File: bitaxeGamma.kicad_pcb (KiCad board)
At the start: 4 copper layers, 56.5 x 99.8 mm, 131 parts, among them J1 54-00164, J2 TC2030-IDC, J3 Conn_01x04, J4 Conn_01x06, J5 USB_C_Receptacle_USB2.0, J6 Conn_01x04, J7 Conn_01x04, SW1 GT-TC029B-H025-L1N, SW2 GT-TC029B-H025-L1N, T1 net-tie, U10 EMC2101, U2 TPS546D24ARVFR, U3 RT9080-33GJ5, U4 ESP32-S3-WROOM-1, U5 MCP1824T-1202E/OT, U6 MCP1824T-0802E, U7 25MHz, U8 BM1370_mode1, U9 SN74AVC4T774

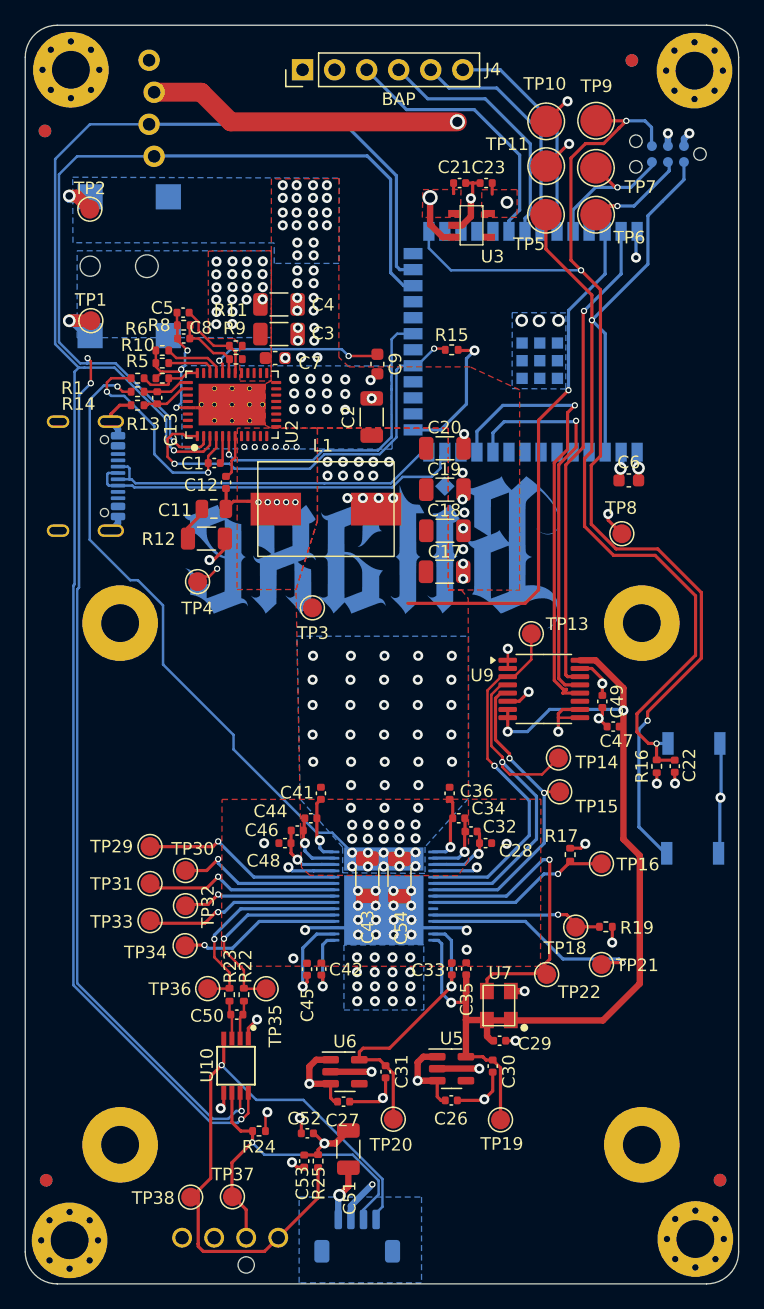
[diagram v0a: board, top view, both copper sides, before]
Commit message: remove incorrect J3 partno for #28. removed random dust from mounting hole positions for #32. bumped version to 603. added NRSTO pulldown. added NRSTI pulldown for #36. removed old manufacturing files.
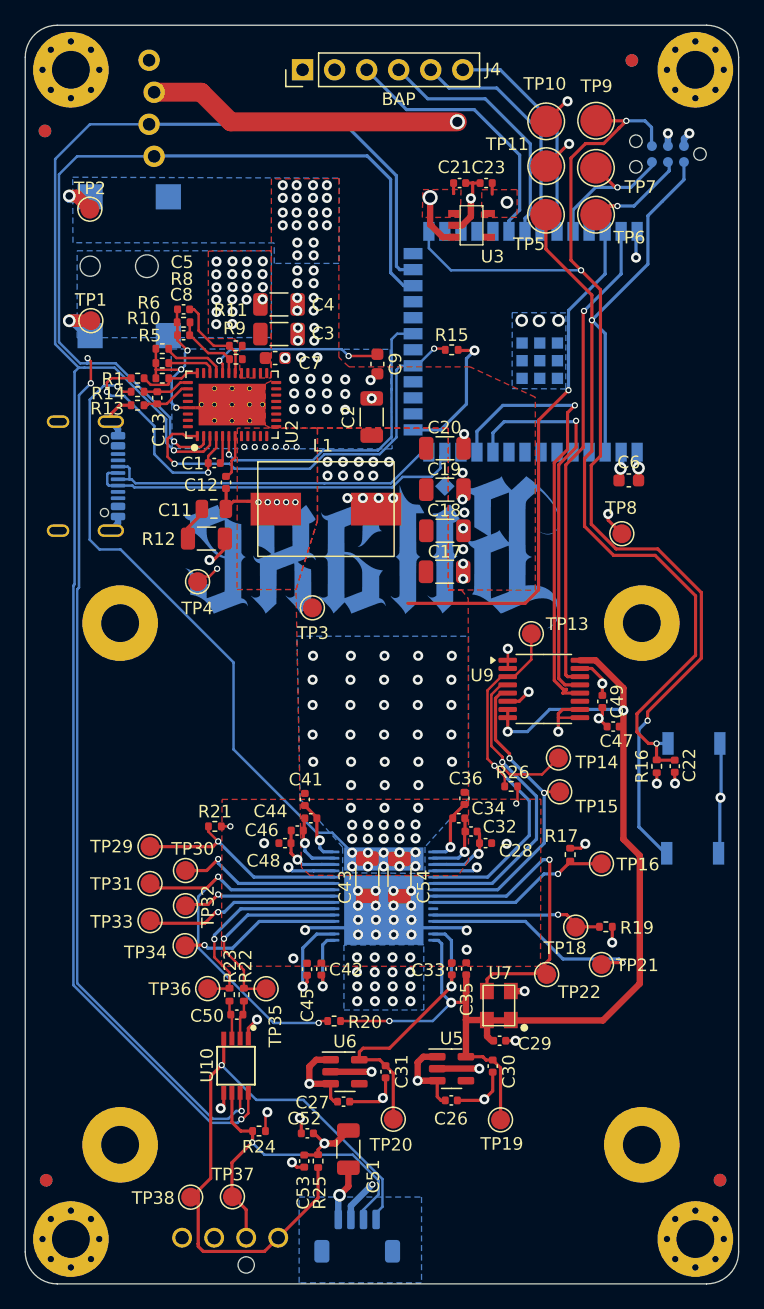
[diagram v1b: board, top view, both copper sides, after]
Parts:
- added R20: 1k, Resistor_SMD:R_0402_1005Metric, F.Cu at (101.7, 126.5)
- added R21: 2k, Resistor_SMD:R_0402_1005Metric, F.Cu at (92.2, 111.0)
- added R26: 10k, Resistor_SMD:R_0402_1005Metric, F.Cu at (115.7, 107.8)
- moved C41 1.37 mm to (99.3, 108.9)
- moved C36 1.24 mm to (112.0, 108.8)
- moved C5 0.26 mm to (89.7, 70.0)
- moved C8 0.26 mm to (89.7, 72.1)
- moved R8 0.24 mm to (89.7, 71.1)
- moved H4 0.15 mm to (80.8, 143.7)
- moved R6 0.14 mm to (88.0, 73.2)
- moved H1 0.09 mm to (130.3, 51.1)
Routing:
- net /BM1370/RI: track 15.5 -> 34.6 mm, vias 1 -> 2
- net /BM1370/1V2: track 77.1 -> 86.5 mm, vias 3 -> 4
- net GND: track 88.7 -> 90.8 mm, vias 126 -> 128
- net /BM1370/RST_N: track 28.4 -> 30.3 mm
- net /BM1370/NRSTO: track 16.1 -> 17.6 mm
- net /VDD: track 91.0 -> 91.6 mm
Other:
- board text added: "603"
- board text removed: "602"

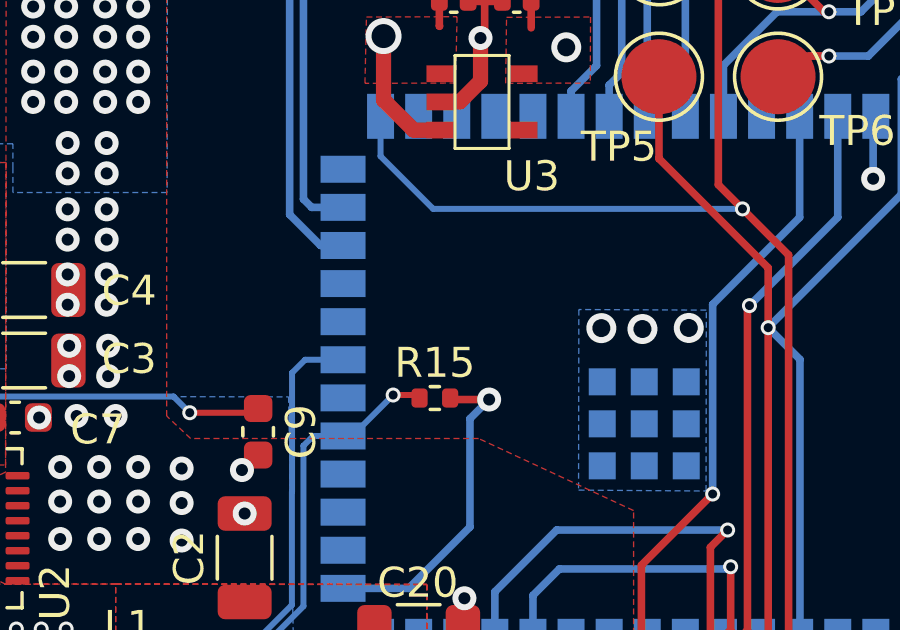
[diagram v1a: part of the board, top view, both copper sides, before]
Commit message: added pullup resistors for #25
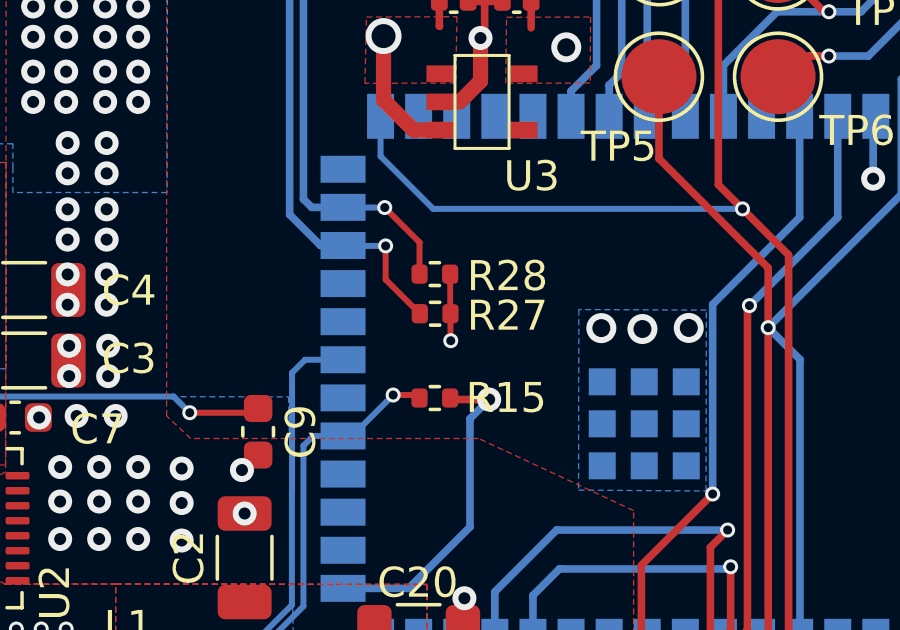
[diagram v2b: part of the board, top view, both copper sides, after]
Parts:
- added R27: 5.6k, Resistor_SMD:R_0402_1005Metric, F.Cu at (111.0, 70.4)
- added R28: 5.6k, Resistor_SMD:R_0402_1005Metric, F.Cu at (111.0, 69.1)
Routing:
- net /SDA: track 137.3 -> 141.5 mm, vias 4 -> 5
- net /SCL: track 140.1 -> 144.1 mm, vias 2 -> 3
- net /3V3: track 53.0 -> 55.2 mm, vias 11 -> 12

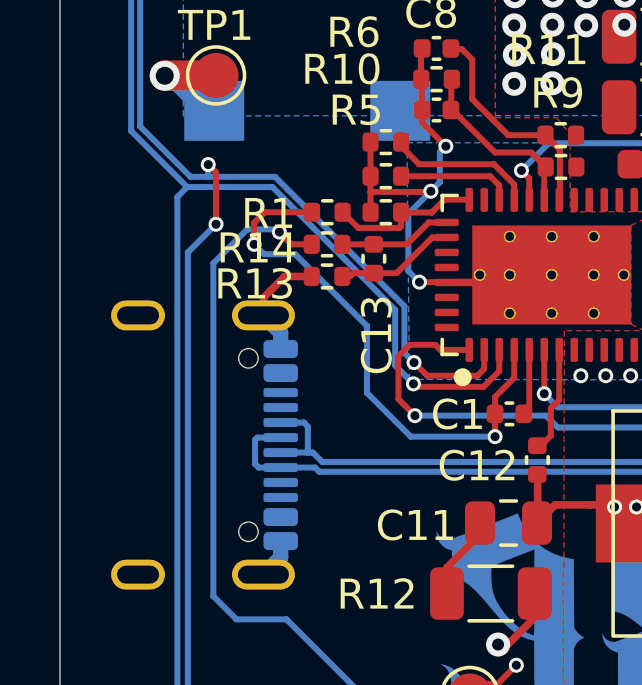
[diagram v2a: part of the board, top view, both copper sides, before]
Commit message: added USB ID pulldown resistors for #37
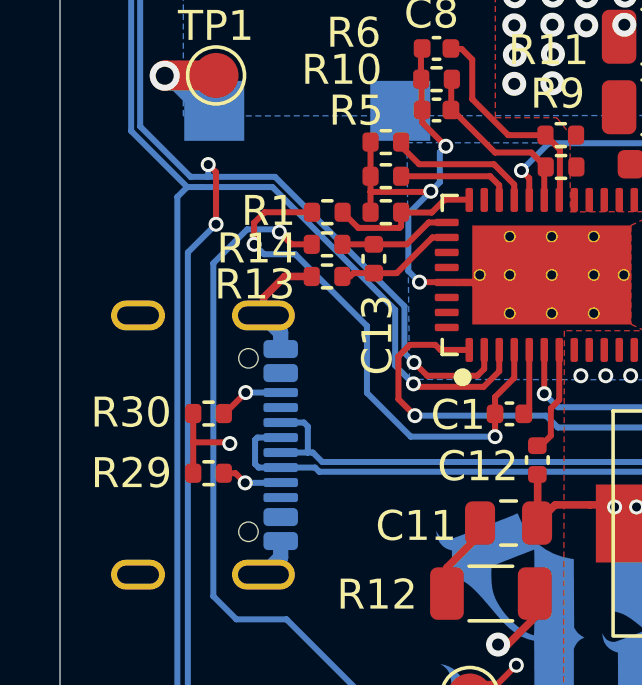
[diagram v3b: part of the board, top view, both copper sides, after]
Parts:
- added R29: 5.1k, Resistor_SMD:R_0402_1005Metric, F.Cu at (82.1, 84.2)
- added R30: 5.1k, Resistor_SMD:R_0402_1005Metric, F.Cu at (82.1, 82.2)
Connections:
- J5 pad A5: unconnected-(J5-CC1-PadA5) -> Net-(J5-CC1)
- J5 pad B5: unconnected-(J5-CC2-PadB5) -> Net-(J5-CC2)
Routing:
- net GND: track 90.8 -> 94.1 mm, vias 128 -> 129
- net Net-(J5-CC2): track 0.00 -> 2.18 mm, vias 0 -> 1
- net Net-(J5-CC1): track 0.00 -> 2.03 mm, vias 0 -> 1

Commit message: removed unused fan header
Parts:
- removed J7: Conn_01x04, Connector_JST:JST_SH_BM04B-SRSS-TB_1x04-1MP_P1.00mm_Vertical
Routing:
- net /Fan/FAN_PWM: track 50.7 -> 31.3 mm, vias 1 -> 0
- net /Fan/FAN_TACH: track 28.2 -> 13.9 mm, vias 1 -> 0
- net /5V: track 197.8 -> 188.9 mm, vias 26 -> 25
- net GND: track 94.1 -> 90.1 mm, vias 129 -> 128
- removed copper zone on B.Cu, net unconnected-(J7-MountPin-PadMP)

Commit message: silkscreen, drc
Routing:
- net GND: track 90.1 -> 92.5 mm, vias 128 -> 129
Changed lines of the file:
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@@
-		)
-	)
-	(gr_text "TAC"
-		(at 104 139.6 90)
-		(layer "B.SilkS")
-		(effects
-			(font
-				(size 0.5 0.5)
-				(thickness 0.125)
-			)
-			(justify mirror)
 		)
 	)
@@
 		)
 	)
-	(gr_text "GND"
-		(at 102 139.5 90)
-		(layer "B.SilkS")
-		(effects
-			(font
-				(size 0.5 0.5)
-				(thickness 0.125)
-			)
-			(justify mirror)
-		)
-	)
 	(gr_text "PWM"
 		(at 97.265 138.363 90)
@@
 		)
 	)
-	(gr_text "5V"
-		(at 102.9 139.7 90)
-		(layer "B.SilkS")
-		(effects
-			(font
-				(size 0.5 0.5)
-				(thickness 0.125)
-			)
-			(justify mirror)
-		)
-	)
 	(gr_text "∞"
 		(at 108.45 111.19 0)
@@
 		)
 	)
-	(gr_text "PWM"
-		(at 105 139.5 90)
-		(layer "B.SilkS")
-		(effects
-			(font
-				(size 0.5 0.5)
-				(thickness 0.125)
-			)
-			(justify mirror)
-		)
-	)
 	(segment
 		(start 112.64 61.122)
@@
 	)
 	(segment
+		(start 102.8 138.075)
+		(end 102 138.875)
+		(width 0.508)
+		(layer "F.Cu")
+		(net 1)
+	)
+	(segment
 		(start 81.63 83.17)
 		(end 81.63 84.2)
@@
 		(end 105.75 132.34)
 		(width 0.254)
+		(layer "F.Cu")
+		(net 1)
+	)
+	(segment
+		(start 102 138.875)
+		(end 102 140.15)
+		(width 0.508)
 		(layer "F.Cu")
 		(net 1)
@@
 		(layers "F.Cu" "B.Cu")
 		(net 1)
+	)
+	(via
+		(at 102 140.15)
+		(size 0.8)
+		(drill 0.4)
+		(layers "F.Cu" "B.Cu")
+		(net 1)
